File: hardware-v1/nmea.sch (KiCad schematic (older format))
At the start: 24 parts, among them P1 CONN_01X20, U10 MCP2562, U11 SN7534051, U12 INA219

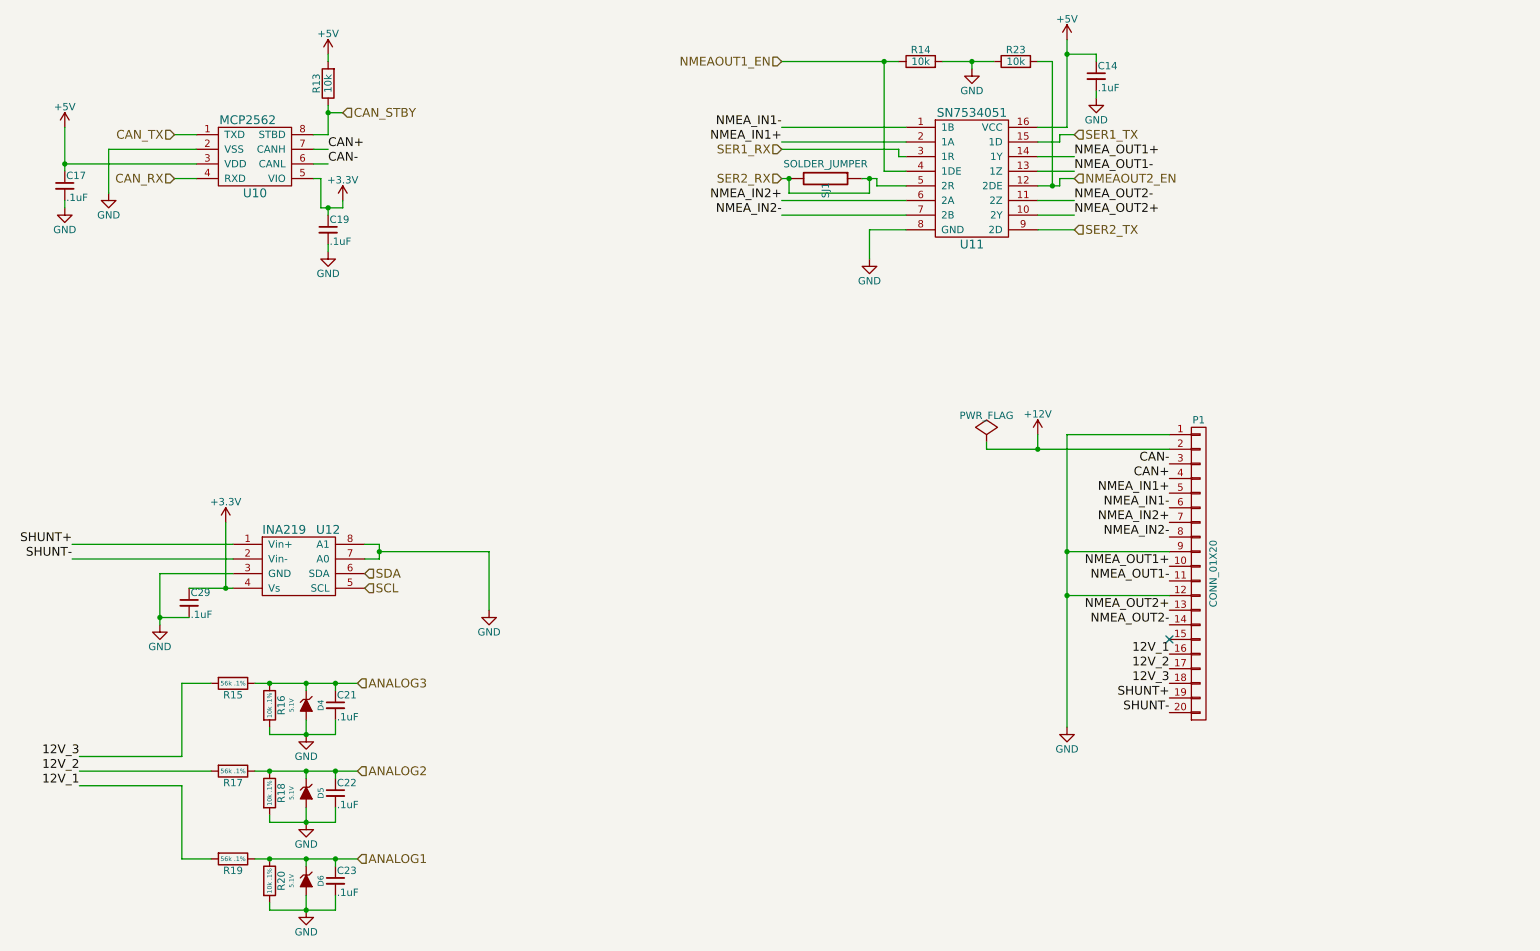
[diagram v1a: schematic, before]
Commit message: remove mcp2562 pull up (there is an internal one)
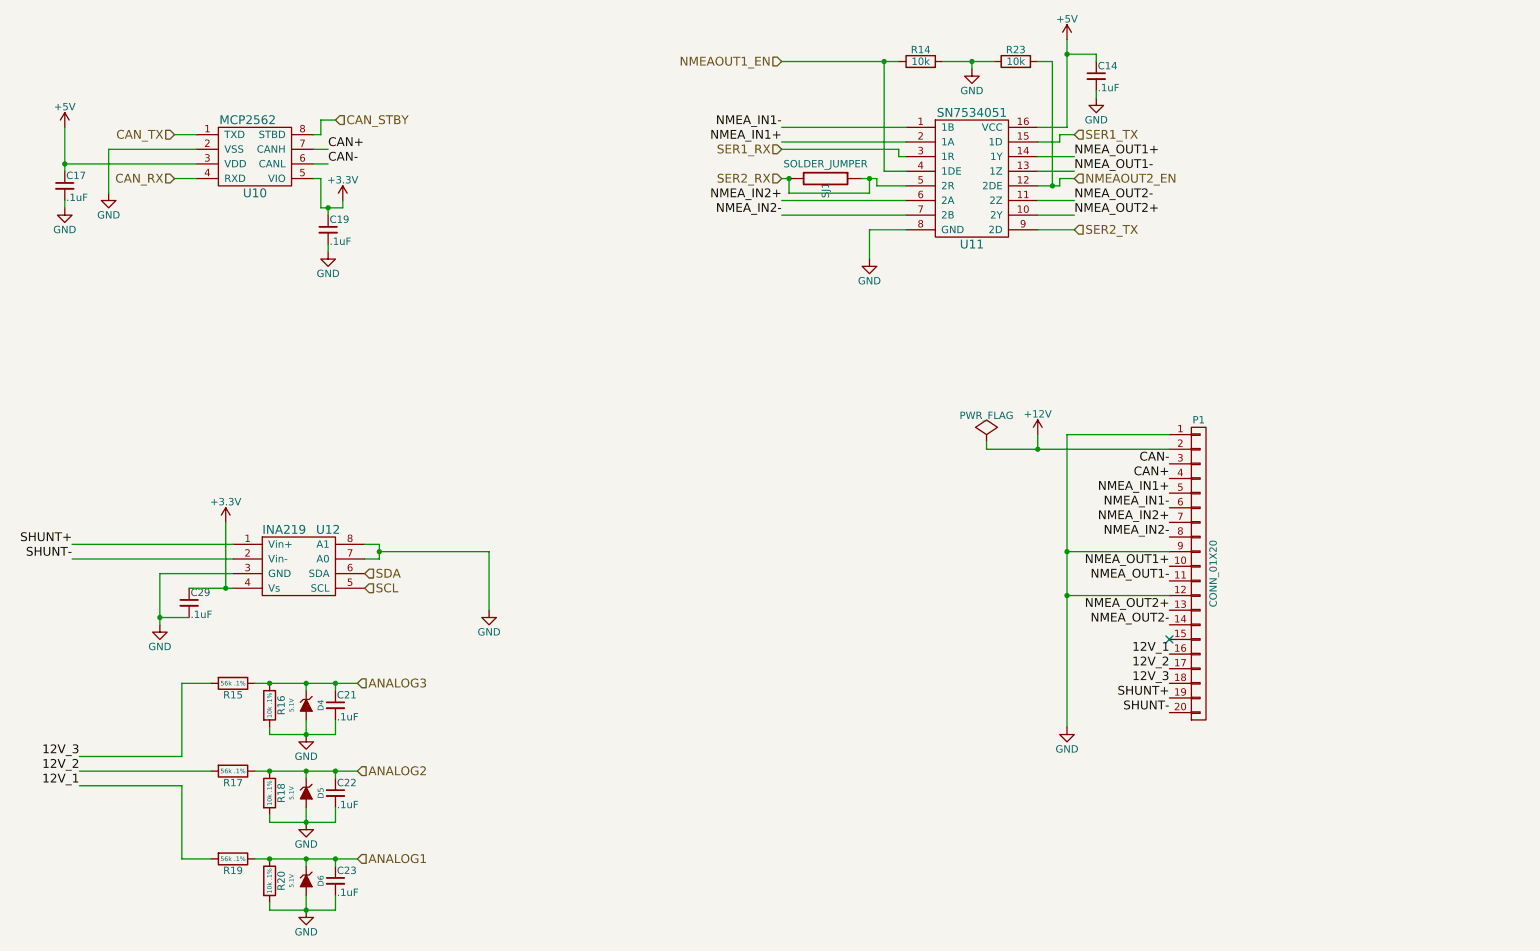
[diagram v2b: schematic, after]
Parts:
- removed R13: 10k, Resistors_SMD:R_0603_HandSoldering, symbol R
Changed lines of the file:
@@
 	1    0    0    -1
 $EndComp
-Text HLabel 3500 1600 2    60   Input ~ 0
+Text HLabel 3450 1650 2    60   Input ~ 0
 CAN_STBY
 $Comp
@@
 F 3 "" H 1600 2250 60  0000 C CNN
 	1    1600 2250
-	1    0    0    -1
-$EndComp
-$Comp
-L R R13
-U 1 1 56635F02
-P 3400 1400
-F 0 "R13" V 3480 1400 50  0000 C CNN
-F 1 "10k" V 3400 1400 50  0000 C CNN
-F 2 "Resistors_SMD:R_0603_HandSoldering" V 3330 1400 30  0001 C CNN
-F 3 "" H 3400 1400 30  0000 C CNN
-	1    3400 1400
-	-1   0    0    1
-$EndComp
-$Comp
-L +5V #PWR061
-U 1 1 56636139
-P 3400 1200
-F 0 "#PWR061" H 3400 1050 50  0001 C CNN
-F 1 "+5V" H 3400 1340 50  0000 C CNN
-F 2 "" H 3400 1200 60  0000 C CNN
-F 3 "" H 3400 1200 60  0000 C CNN
-	1    3400 1200
 	1    0    0    -1
 $EndComp
@@
 	2400 5500 2600 5500
 Wire Wire Line
-	2900 5500 3600 5500
+	2900 5500 3000 5500
+Wire Wire Line
+	3000 5500 3250 5500
+Wire Wire Line
+	3250 5500 3450 5500
+Wire Wire Line
+	3450 5500 3600 5500
 Connection ~ 3000 5500
 Wire Wire Line
@@
 	3000 5800 3000 5850
 Wire Wire Line
-	3000 5850 3450 5850
+	3000 5850 3250 5850
+Wire Wire Line
+	3250 5850 3450 5850
 Connection ~ 3250 5850
 Wire Wire Line
@@
 	2500 1950 1600 1950
 Wire Wire Line
-	1600 1700 1600 2000
-Wire Wire Line
-	3400 1600 3500 1600
-Wire Wire Line
-	3400 1550 3400 1750
-Wire Wire Line
-	3400 1750 3300 1750
-Wire Wire Line
-	3350 2250 3500 2250
+	1600 1700 1600 1950
+Wire Wire Line
+	1600 1950 1600 2000
+Wire Wire Line
+	3350 1750 3300 1750
+Wire Wire Line
+	3350 2250 3400 2250
+Wire Wire Line
+	3400 2250 3500 2250
 Wire Wire Line
 	3400 2300 3400 2250
@@
 	1600 2200 1600 2250
 Connection ~ 1600 1950
-Connection ~ 3400 1600
-Wire Wire Line
-	3400 1200 3400 1250
 Wire Wire Line
 	1700 6100 2600 6100
 Wire Wire Line
-	2900 6100 3600 6100
+	2900 6100 3000 6100
+Wire Wire Line
+	3000 6100 3250 6100
+Wire Wire Line
+	3250 6100 3450 6100
+Wire Wire Line
+	3450 6100 3600 6100
 Connection ~ 3000 6100
 Wire Wire Line
@@
 	3000 6400 3000 6450
 Wire Wire Line
-	3000 6450 3450 6450
+	3000 6450 3250 6450
+Wire Wire Line
+	3250 6450 3450 6450
 Connection ~ 3250 6450
 Wire Wire Line
 	2400 6700 2600 6700
 Wire Wire Line
-	2900 6700 3600 6700
+	2900 6700 3000 6700
+Wire Wire Line
+	3000 6700 3250 6700
+Wire Wire Line
+	3250 6700 3450 6700
+Wire Wire Line
+	3450 6700 3600 6700
 Connection ~ 3000 6700
 Wire Wire Line
@@
 	3000 7000 3000 7050
 Wire Wire Line
-	3000 7050 3450 7050
+	3000 7050 3250 7050
+Wire Wire Line
+	3250 7050 3450 7050
 Connection ~ 3250 7050
 Wire Wire Line
@@
 	2750 4750 2250 4750
 Wire Wire Line
-	2250 4750 2250 5100
-Wire Wire Line
-	2450 4850 2750 4850
+	2250 4750 2250 5050
+Wire Wire Line
+	2250 5050 2250 5100
+Wire Wire Line
+	2450 4850 2700 4850
+Wire Wire Line
+	2700 4850 2750 4850
 Wire Wire Line
 	2700 4850 2700 4400
@@
 	3650 4550 3750 4550
 Wire Wire Line
-	3750 4550 3750 4650
+	3750 4550 3750 4600
+Wire Wire Line
+	3750 4600 3750 4650
 Wire Wire Line
 	3750 4650 3650 4650
@@
 	8450 1700 8250 1700
 Wire Wire Line
-	8450 1100 8450 1700
+	8450 1100 8450 1200
+Wire Wire Line
+	8450 1200 8450 1700
 Wire Wire Line
 	8450 1200 8650 1200
@@
 	7100 2400 7100 2600
 Wire Wire Line
-	8250 2100 8400 2100
+	8250 2100 8350 2100
+Wire Wire Line
+	8350 2100 8400 2100
 Wire Wire Line
 	6500 2200 7350 2200
@@
 	7300 1850 6500 1850
 Wire Wire Line
-	6500 1250 7300 1250
+	6500 1250 7200 1250
+Wire Wire Line
+	7200 1250 7300 1250
 Wire Wire Line
 	7200 1250 7200 2000
@@
 Connection ~ 7200 1250
 Wire Wire Line
-	7600 1250 7950 1250
+	7600 1250 7800 1250
+Wire Wire Line
+	7800 1250 7950 1250
 Wire Wire Line
 	7800 1250 7800 1300
@@
 	7150 2050 7150 2100
 Wire Wire Line
-	7050 2050 7150 2050
-Wire Wire Line
-	7900 3900 9150 3900
+	7050 2050 7100 2050
+Wire Wire Line
+	7100 2050 7150 2050
+Wire Wire Line
+	7900 3900 8250 3900
+Wire Wire Line
+	8250 3900 9150 3900
 Wire Wire Line
 	8250 3900 8250 3800
@@
 	8450 4900 9150 4900
 Wire Wire Line
-	8450 3800 8450 5800
+	8450 3800 8450 4600
+Wire Wire Line
+	8450 4600 8450 4900
+Wire Wire Line
+	8450 4900 8450 5800
 Connection ~ 8450 4600
 Connection ~ 8450 4900
@@
 Connection ~ 7100 2050
 Connection ~ 6550 2050
+Wire Wire Line
+	3350 1750 3350 1650
+Wire Wire Line
+	3350 1650 3450 1650
 $EndSCHEMATC

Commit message: invert nmea signals
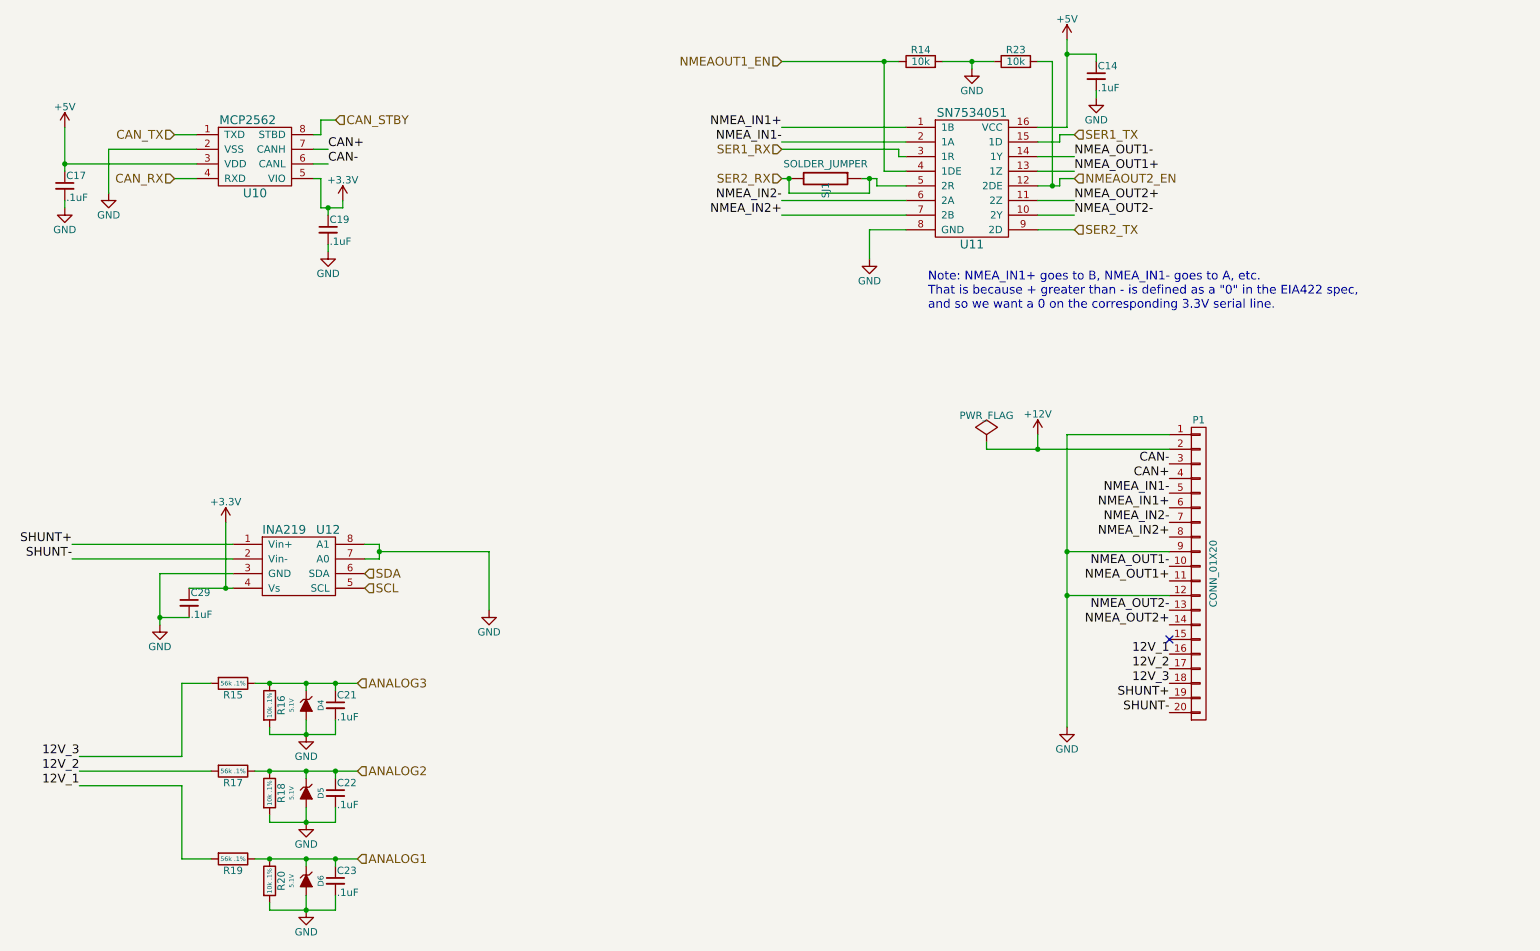
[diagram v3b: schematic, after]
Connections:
- net NMEA_IN1+: now also P1.6 (P6), U11.1 (1B); no longer P1.5 (P5), U11.2 (1A)
- net NMEA_IN1-: now also P1.5 (P5), U11.2 (1A); no longer P1.6 (P6), U11.1 (1B)
- net NMEA_IN2+: now also P1.8 (P8), U11.7 (2B); no longer P1.7 (P7), U11.6 (2A)
- net NMEA_IN2-: now also P1.7 (P7), U11.6 (2A); no longer P1.8 (P8), U11.7 (2B)
- net NMEA_OUT1+: now also P1.11 (P11), U11.13 (1Z); no longer P1.10 (P10), U11.14 (1Y)
- net NMEA_OUT1-: now also P1.10 (P10), U11.14 (1Y); no longer P1.11 (P11), U11.13 (1Z)
- net NMEA_OUT2+: now also P1.14 (P14), U11.11 (2Z); no longer P1.13 (P13), U11.10 (2Y)
- net NMEA_OUT2-: now also P1.13 (P13), U11.10 (2Y); no longer P1.14 (P14), U11.11 (2Z)
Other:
- note added: "Note: NMEA_IN1+ goes to B, NMEA_IN1- goes to A, etc.\nThat is because + greater than - is defined as a "0" in the EIA422 spec, \nand so we want a 0 on the corresponding 3.3V serial line."
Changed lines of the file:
@@
 Wire Wire Line
 	8250 1900 8500 1900
+Text Label 6500 1700 2    60   ~ 0
+NMEA_IN1+
 Text Label 6500 1800 2    60   ~ 0
-NMEA_IN1+
-Text Label 6500 1700 2    60   ~ 0
 NMEA_IN1-
+Text Label 6500 2300 2    60   ~ 0
+NMEA_IN2+
 Text Label 6500 2200 2    60   ~ 0
-NMEA_IN2+
-Text Label 6500 2300 2    60   ~ 0
 NMEA_IN2-
+Text Label 8500 2000 0    60   ~ 0
+NMEA_OUT1+
 Text Label 8500 1900 0    60   ~ 0
-NMEA_OUT1+
-Text Label 8500 2000 0    60   ~ 0
 NMEA_OUT1-
+Text Label 8500 2300 0    60   ~ 0
+NMEA_OUT2-
 Text Label 8500 2200 0    60   ~ 0
-NMEA_OUT2-
-Text Label 8500 2300 0    60   ~ 0
 NMEA_OUT2+
 Wire Wire Line
@@
 Text Label 9150 4000 2    60   ~ 0
 CAN-
+Text Label 9150 4300 2    60   ~ 0
+NMEA_IN1+
 Text Label 9150 4200 2    60   ~ 0
-NMEA_IN1+
-Text Label 9150 4300 2    60   ~ 0
 NMEA_IN1-
+Text Label 9150 4500 2    60   ~ 0
+NMEA_IN2+
 Text Label 9150 4400 2    60   ~ 0
-NMEA_IN2+
-Text Label 9150 4500 2    60   ~ 0
 NMEA_IN2-
+Text Label 9150 4800 2    60   ~ 0
+NMEA_OUT1+
 Text Label 9150 4700 2    60   ~ 0
-NMEA_OUT1+
-Text Label 9150 4800 2    60   ~ 0
 NMEA_OUT1-
+Text Label 9150 5100 2    60   ~ 0
+NMEA_OUT2+
 Text Label 9150 5000 2    60   ~ 0
-NMEA_OUT2+
-Text Label 9150 5100 2    60   ~ 0
 NMEA_OUT2-
 Text Label 9150 5300 2    60   ~ 0
@@
 Wire Wire Line
 	3350 1650 3450 1650
+Text Notes 7500 2950 0    60   ~ 0
+Note: NMEA_IN1+ goes to B, NMEA_IN1- goes to A, etc.\nThat is because + greater than - is defined as a "0" in the EIA422 spec, \nand so we want a 0 on the corresponding 3.3V serial line.
 $EndSCHEMATC

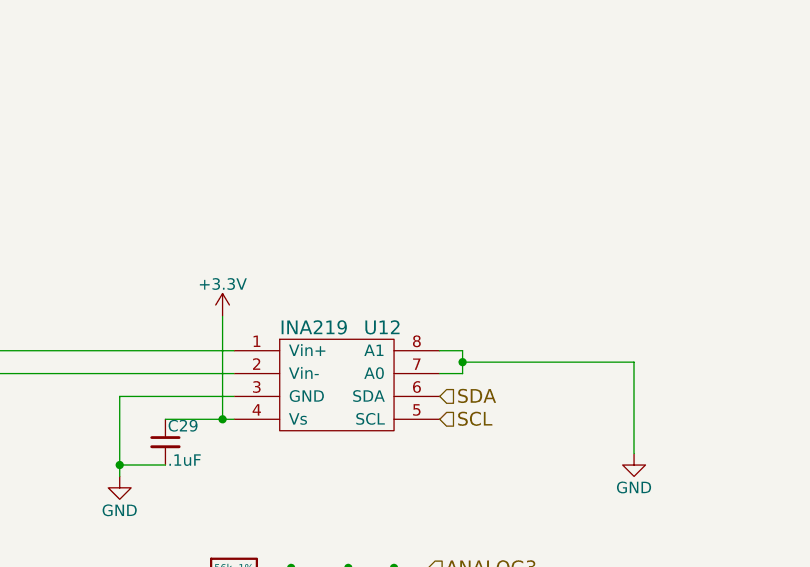
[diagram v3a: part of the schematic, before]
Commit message: Add i2c addresses on schematic
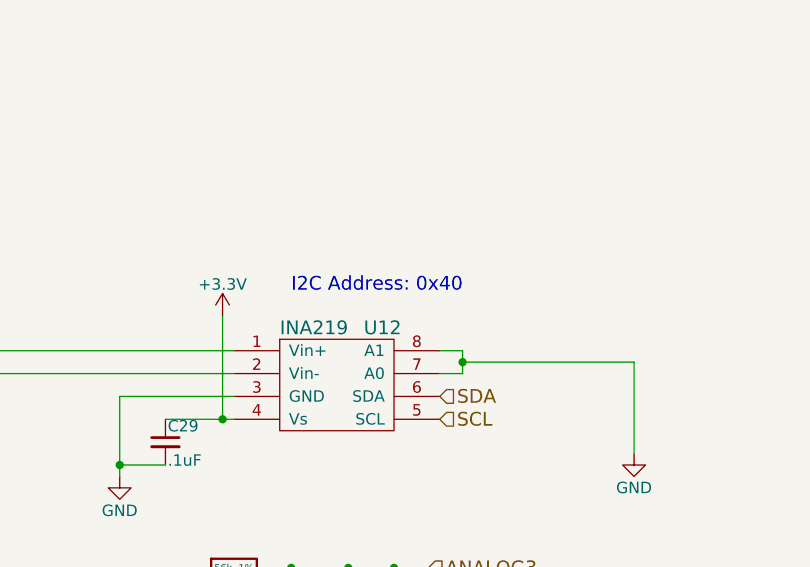
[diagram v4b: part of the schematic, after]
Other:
- note added: "I2C Address: 0x40"
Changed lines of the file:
@@
 Text Notes 7500 2950 0    60   ~ 0
 Note: NMEA_IN1+ goes to B, NMEA_IN1- goes to A, etc.\nThat is because + greater than - is defined as a "0" in the EIA422 spec, \nand so we want a 0 on the corresponding 3.3V serial line.
+Text Notes 3000 4300 0    60   ~ 0
+I2C Address: 0x40
 $EndSCHEMATC
